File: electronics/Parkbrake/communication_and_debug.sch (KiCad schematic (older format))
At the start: 18 parts

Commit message: ordernr, type and footprints for all components
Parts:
- C? (x3): footprint (none) -> Capacitors_SMD:C_0805; farnell (none) -> 2496940; part (none) -> 0805B104J500CT
- C?: footprint (none) -> Capacitors_SMD:C_0805; farnell (none) -> 2494247; part (none) -> GRM2165C1H102JA01D
- R?: farnell (none) -> 9332480; part (none) -> MC01W08051120R
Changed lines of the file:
@@
 F 0 "C?" H 2475 3550 50  0000 L CNN
 F 1 "100n" H 2475 3350 50  0000 L CNN
-F 2 "" H 2488 3300 50  0000 C CNN
+F 2 "Capacitors_SMD:C_0805" H 2488 3300 50  0001 C CNN
 F 3 "" H 2450 3450 50  0000 C CNN
+F 4 "2496940" H 2450 3450 60  0001 C CNN "farnell"
+F 5 "0805B104J500CT" H 2450 3450 60  0001 C CNN "part"
 	1    2450 3450
 	1    0    0    -1
@@
 F 0 "C?" H 2725 3550 50  0000 L CNN
 F 1 "1n" H 2725 3350 50  0000 L CNN
-F 2 "" H 2738 3300 50  0000 C CNN
+F 2 "Capacitors_SMD:C_0805" H 2738 3300 50  0001 C CNN
 F 3 "" H 2700 3450 50  0000 C CNN
+F 4 "2494247" H 2700 3450 60  0001 C CNN "farnell"
+F 5 "GRM2165C1H102JA01D" H 2700 3450 60  0001 C CNN "part"
 	1    2700 3450
 	1    0    0    -1
@@
 F 0 "C?" H 3450 4525 50  0000 L CNN
 F 1 "100n" H 3450 4325 50  0000 L CNN
-F 2 "" H 3463 4275 50  0000 C CNN
+F 2 "Capacitors_SMD:C_0805" H 3463 4275 50  0001 C CNN
 F 3 "" H 3425 4425 50  0000 C CNN
+F 4 "2496940" H 3425 4425 60  0001 C CNN "farnell"
+F 5 "0805B104J500CT" H 3425 4425 60  0001 C CNN "part"
 	1    3425 4425
 	1    0    0    -1
@@
 F 2 "" V 3505 4050 50  0000 C CNN
 F 3 "" H 3575 4050 50  0000 C CNN
+F 4 "MC01W08051120R" V 3575 4050 60  0001 C CNN "part"
+F 5 "9332480" V 3575 4050 60  0001 C CNN "farnell"
 	1    3575 4050
 	1    0    0    -1
@@
 F 0 "C?" H 7900 5200 50  0000 L CNN
 F 1 "100n" H 7900 5000 50  0000 L CNN
-F 2 "" H 7913 4950 50  0000 C CNN
+F 2 "Capacitors_SMD:C_0805" H 7913 4950 50  0001 C CNN
 F 3 "" H 7875 5100 50  0000 C CNN
+F 4 "2496940" H 7875 5100 60  0001 C CNN "farnell"
+F 5 "0805B104J500CT" H 7875 5100 60  0001 C CNN "part"
 	1    7875 5100
 	1    0    0    -1

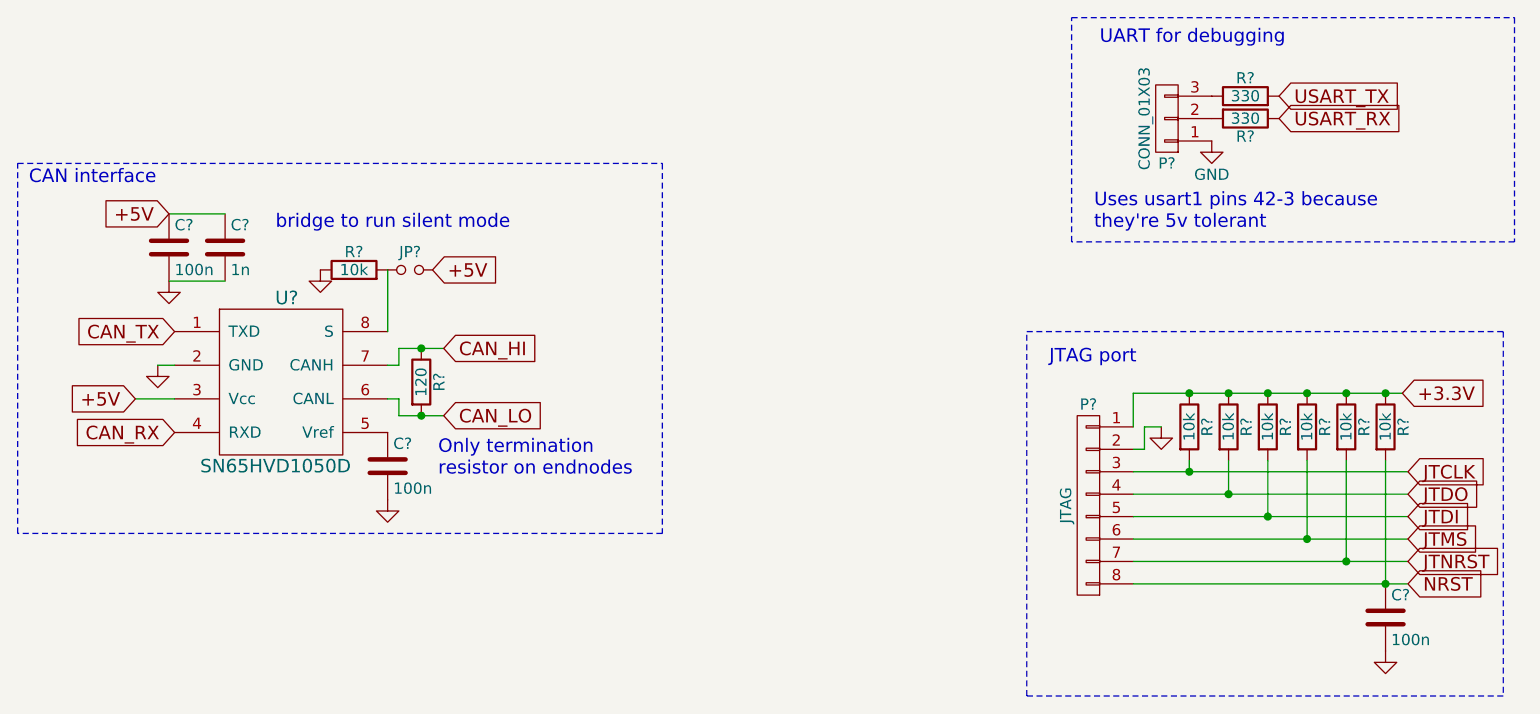
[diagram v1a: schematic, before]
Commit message: Make it pass DRC rule check
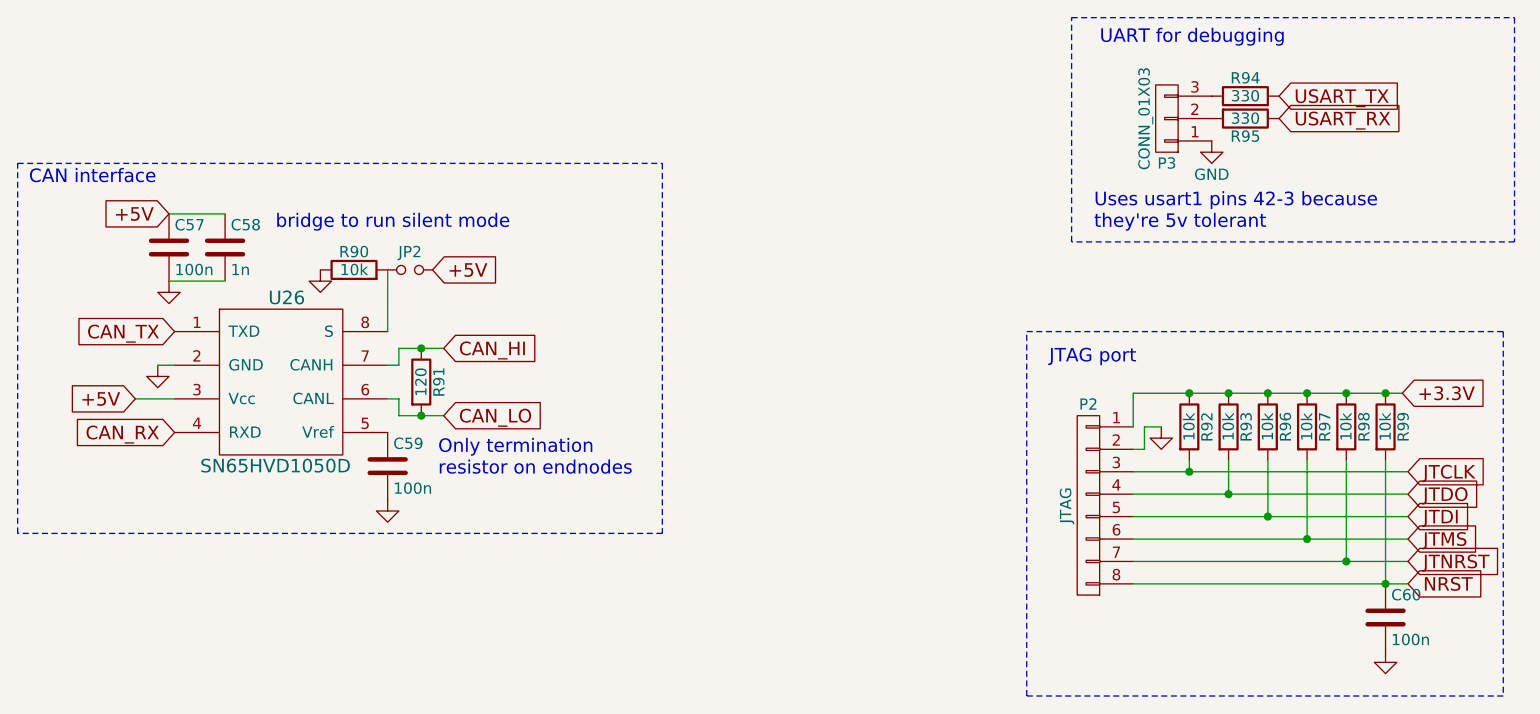
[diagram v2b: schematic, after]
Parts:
- gave numbers to parts that had none: 18
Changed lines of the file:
@@
 $EndDescr
 $Comp
-L SN65HVD1050D U?
+L SN65HVD1050D U26
 U 1 1 5791E80E
 P 2925 4025
-F 0 "U?" H 2975 4375 60  0000 C CNN
+F 0 "U26" H 2975 4375 60  0000 C CNN
 F 1 "SN65HVD1050D" H 2925 3625 60  0000 C CNN
 F 2 "Housings_SOIC:SOIC-8_3.9x4.9mm_Pitch1.27mm" H 3025 3875 60  0001 C CNN
@@
 $EndComp
 $Comp
-L R R?
+L R R90
 U 1 1 5791E8BD
 P 3275 3550
-F 0 "R?" V 3355 3550 50  0000 C CNN
+F 0 "R90" V 3355 3550 50  0000 C CNN
 F 1 "10k" V 3275 3550 50  0000 C CNN
 F 2 "Resistors_SMD:R_0805" V 3205 3550 50  0001 C CNN
@@
 $EndComp
 $Comp
-L Jumper_NO_Small JP?
+L Jumper_NO_Small JP2
 U 1 1 5791E904
 P 3525 3550
-F 0 "JP?" H 3525 3630 50  0000 C CNN
+F 0 "JP2" H 3525 3630 50  0000 C CNN
 F 1 "Jumper_NO_Small" H 3535 3490 50  0001 C CNN
 F 2 "" H 3525 3550 50  0000 C CNN
@@
 $EndComp
 $Comp
-L GND #PWR?
+L GND #PWR082
 U 1 1 5791E9C0
 P 3125 3550
-F 0 "#PWR?" H 3125 3300 50  0001 C CNN
+F 0 "#PWR082" H 3125 3300 50  0001 C CNN
 F 1 "GND" H 3125 3400 50  0001 C CNN
 F 2 "" H 3125 3550 50  0000 C CNN
@@
 $EndComp
 $Comp
-L C C?
+L C C57
 U 1 1 5791E9E8
 P 2450 3450
-F 0 "C?" H 2475 3550 50  0000 L CNN
+F 0 "C57" H 2475 3550 50  0000 L CNN
 F 1 "100n" H 2475 3350 50  0000 L CNN
 F 2 "Capacitors_SMD:C_0805" H 2488 3300 50  0001 C CNN
@@
 $EndComp
 $Comp
-L C C?
+L C C58
 U 1 1 5791EA0D
 P 2700 3450
-F 0 "C?" H 2725 3550 50  0000 L CNN
+F 0 "C58" H 2725 3550 50  0000 L CNN
 F 1 "1n" H 2725 3350 50  0000 L CNN
 F 2 "Capacitors_SMD:C_0805" H 2738 3300 50  0001 C CNN
@@
 	2700 3600 2450 3600
 $Comp
-L GND #PWR?
+L GND #PWR083
 U 1 1 5791EA76
 P 2450 3600
-F 0 "#PWR?" H 2450 3350 50  0001 C CNN
+F 0 "#PWR083" H 2450 3350 50  0001 C CNN
 F 1 "GND" H 2450 3450 50  0001 C CNN
 F 2 "" H 2450 3600 50  0000 C CNN
@@
 +5V
 $Comp
-L GND #PWR?
+L GND #PWR084
 U 1 1 5791EABC
 P 2400 3975
-F 0 "#PWR?" H 2400 3725 50  0001 C CNN
+F 0 "#PWR084" H 2400 3725 50  0001 C CNN
 F 1 "GND" H 2400 3825 50  0001 C CNN
 F 2 "" H 2400 3975 50  0000 C CNN
@@
 	2475 4125 2300 4125
 $Comp
-L C C?
+L C C59
 U 1 1 5791EB00
 P 3425 4425
-F 0 "C?" H 3450 4525 50  0000 L CNN
+F 0 "C59" H 3450 4525 50  0000 L CNN
 F 1 "100n" H 3450 4325 50  0000 L CNN
 F 2 "Capacitors_SMD:C_0805" H 3463 4275 50  0001 C CNN
@@
 $EndComp
 $Comp
-L GND #PWR?
+L GND #PWR085
 U 1 1 5791EB6A
 P 3425 4575
-F 0 "#PWR?" H 3425 4325 50  0001 C CNN
+F 0 "#PWR085" H 3425 4325 50  0001 C CNN
 F 1 "GND" H 3425 4425 50  0001 C CNN
 F 2 "" H 3425 4575 50  0000 C CNN
@@
 bridge to run silent mode
 $Comp
-L R R?
+L R R91
 U 1 1 5791F232
 P 3575 4050
-F 0 "R?" V 3655 4050 50  0000 C CNN
+F 0 "R91" V 3655 4050 50  0000 C CNN
 F 1 "120" V 3575 4050 50  0000 C CNN
 F 2 "" V 3505 4050 50  0000 C CNN
@@
 Connection ~ 3575 3900
 $Comp
-L CONN_01X03 P?
+L CONN_01X03 P3
 U 1 1 57920C75
 P 6900 2875
-F 0 "P?" H 6900 3075 50  0000 C CNN
+F 0 "P3" H 6900 3075 50  0000 C CNN
 F 1 "CONN_01X03" V 7000 2875 50  0000 C CNN
 F 2 "" H 6900 2875 50  0000 C CNN
@@
 $EndComp
 $Comp
-L R R?
+L R R94
 U 1 1 57920D82
 P 7250 2775
-F 0 "R?" V 7330 2775 50  0000 C CNN
+F 0 "R94" V 7330 2775 50  0000 C CNN
 F 1 "330" V 7250 2775 50  0000 C CNN
 F 2 "" V 7180 2775 50  0000 C CNN
@@
 $EndComp
 $Comp
-L R R?
+L R R95
 U 1 1 57920DB5
 P 7250 2875
-F 0 "R?" V 7330 2875 50  0000 C CNN
+F 0 "R95" V 7330 2875 50  0000 C CNN
 F 1 "330" V 7250 2875 50  0000 C CNN
 F 2 "" V 7180 2875 50  0000 C CNN
@@
 $EndComp
 $Comp
-L GND #PWR?
+L GND #PWR086
 U 1 1 57920F20
 P 7100 2975
-F 0 "#PWR?" H 7100 2725 50  0001 C CNN
+F 0 "#PWR086" H 7100 2725 50  0001 C CNN
 F 1 "GND" H 7100 2825 50  0000 C CNN
 F 2 "" H 7100 2975 50  0000 C CNN
@@
 	6475 3425 6475 2425
 $Comp
-L GND #PWR?
+L GND #PWR087
 U 1 1 579225C8
 P 6875 4250
-F 0 "#PWR?" H 6875 4000 50  0001 C CNN
+F 0 "#PWR087" H 6875 4000 50  0001 C CNN
 F 1 "GND" H 6875 4100 50  0001 C CNN
 F 2 "" H 6875 4250 50  0000 C CNN
@@
 +3.3V
 $Comp
-L CONN_01X08 P?
+L CONN_01X08 P2
 U 1 1 57922780
 P 6550 4600
-F 0 "P?" H 6550 5050 50  0000 C CNN
+F 0 "P2" H 6550 5050 50  0000 C CNN
 F 1 "JTAG" V 6650 4600 50  0000 C CNN
 F 2 "" H 6550 4600 50  0000 C CNN
@@
 JTAG port
 $Comp
-L R R?
+L R R92
 U 1 1 5792478C
 P 7000 4250
-F 0 "R?" V 7080 4250 50  0000 C CNN
+F 0 "R92" V 7080 4250 50  0000 C CNN
 F 1 "10k" V 7000 4250 50  0000 C CNN
 F 2 "Resistors_SMD:R_0805" V 6930 4250 50  0001 C CNN
@@
 	6800 4250 6875 4250
 $Comp
-L R R?
+L R R93
 U 1 1 57924D13
 P 7175 4250
-F 0 "R?" V 7255 4250 50  0000 C CNN
+F 0 "R93" V 7255 4250 50  0000 C CNN
 F 1 "10k" V 7175 4250 50  0000 C CNN
 F 2 "Resistors_SMD:R_0805" V 7105 4250 50  0001 C CNN
@@
 $EndComp
 $Comp
-L R R?
+L R R96
 U 1 1 57924D64
 P 7350 4250
-F 0 "R?" V 7430 4250 50  0000 C CNN
+F 0 "R96" V 7430 4250 50  0000 C CNN
 F 1 "10k" V 7350 4250 50  0000 C CNN
 F 2 "Resistors_SMD:R_0805" V 7280 4250 50  0001 C CNN
@@
 $EndComp
 $Comp
-L R R?
+L R R97
 U 1 1 57924DA8
 P 7525 4250
-F 0 "R?" V 7605 4250 50  0000 C CNN
+F 0 "R97" V 7605 4250 50  0000 C CNN
 F 1 "10k" V 7525 4250 50  0000 C CNN
 F 2 "Resistors_SMD:R_0805" V 7455 4250 50  0001 C CNN
@@
 $EndComp
 $Comp
-L R R?
+L R R98
 U 1 1 57924E03
 P 7700 4250
-F 0 "R?" V 7780 4250 50  0000 C CNN
+F 0 "R98" V 7780 4250 50  0000 C CNN
 F 1 "10k" V 7700 4250 50  0000 C CNN
 F 2 "Resistors_SMD:R_0805" V 7630 4250 50  0001 C CNN
@@
 Connection ~ 7700 4850
 $Comp
-L R R?
+L R R99
 U 1 1 5792546C
 P 7875 4250
-F 0 "R?" V 7955 4250 50  0000 C CNN
+F 0 "R99" V 7955 4250 50  0000 C CNN
 F 1 "10k" V 7875 4250 50  0000 C CNN
 F 2 "Resistors_SMD:R_0805" V 7805 4250 50  0001 C CNN
@@
 Connection ~ 7875 4100
 $Comp
-L C C?
+L C C60
 U 1 1 579264A6
 P 7875 5100
-F 0 "C?" H 7900 5200 50  0000 L CNN
+F 0 "C60" H 7900 5200 50  0000 L CNN
 F 1 "100n" H 7900 5000 50  0000 L CNN
 F 2 "Capacitors_SMD:C_0805" H 7913 4950 50  0001 C CNN
@@
 $EndComp
 $Comp
-L GND #PWR?
+L GND #PWR088
 U 1 1 579264FD
 P 7875 5250
-F 0 "#PWR?" H 7875 5000 50  0001 C CNN
+F 0 "#PWR088" H 7875 5000 50  0001 C CNN
 F 1 "GND" H 7875 5100 50  0001 C CNN
 F 2 "" H 7875 5250 50  0000 C CNN

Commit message: More fixes and chenged components eat less boardspace
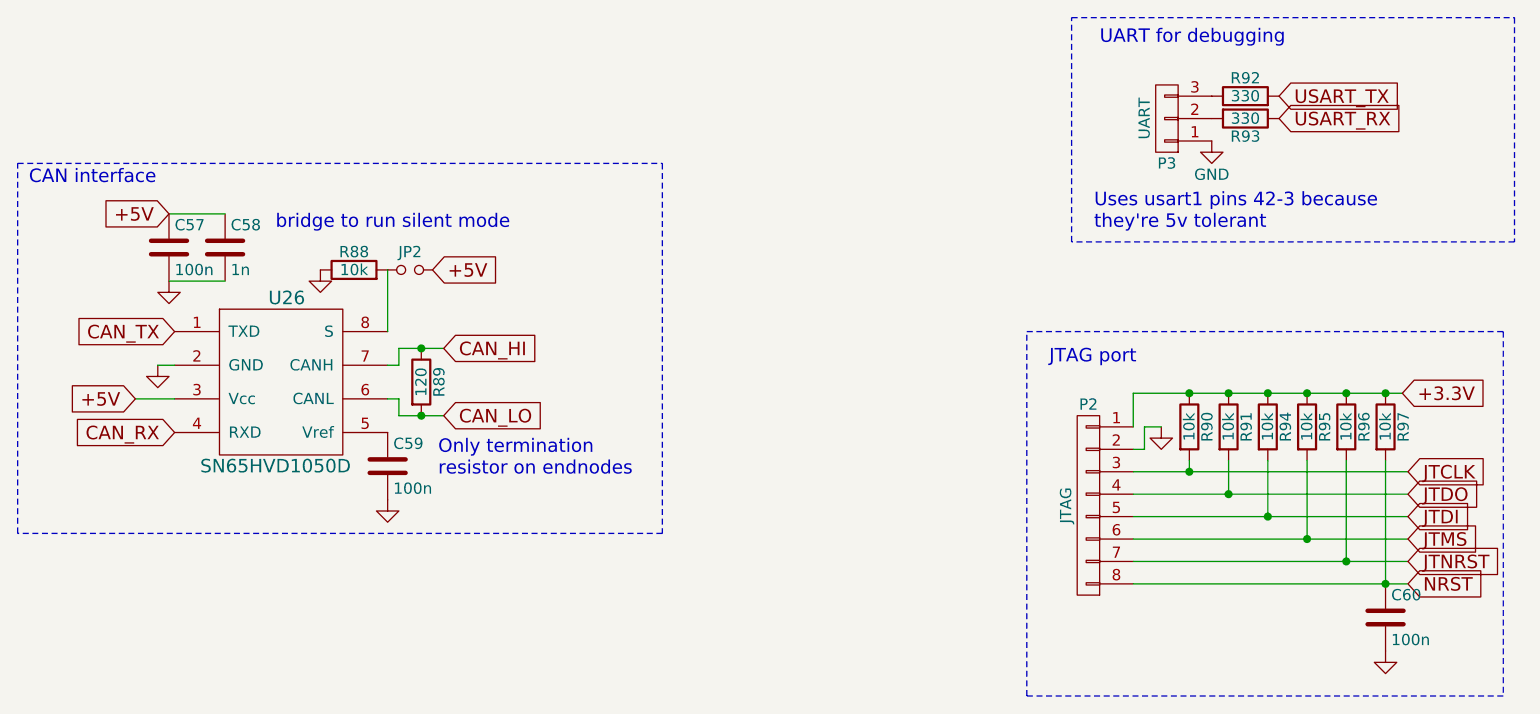
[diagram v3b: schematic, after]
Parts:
- JP2: footprint (none) -> Resistors_SMD:R_0805_HandSoldering; farnell (none) -> 9240276; part (none) -> RC1206JR-070RL
- P2: footprint (none) -> Socket_Strips:Socket_Strip_Straight_1x08; farnell (none) -> 2356160; part (none) -> 61300811121
- P3: value CONN_01X03 -> UART; footprint (none) -> Socket_Strips:Socket_Strip_Straight_1x03; farnell (none) -> 3418297; part (none) -> 826629-3
- R89: renamed from R91; footprint (none) -> Resistors_SMD:R_0805
- R92: renamed from R94; footprint (none) -> Resistors_SMD:R_0805
- R93: renamed from R95; footprint (none) -> Resistors_SMD:R_0805
- renumbered R90 to R88, R92 to R90, R93 to R91, R96 to R94, R97 to R95, R98 to R96, R99 to R97
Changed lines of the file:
@@
 $EndComp
 $Comp
-L R R90
+L R R88
 U 1 1 5791E8BD
 P 3275 3550
-F 0 "R90" V 3355 3550 50  0000 C CNN
+F 0 "R88" V 3355 3550 50  0000 C CNN
 F 1 "10k" V 3275 3550 50  0000 C CNN
 F 2 "Resistors_SMD:R_0805" V 3205 3550 50  0001 C CNN
@@
 F 0 "JP2" H 3525 3630 50  0000 C CNN
 F 1 "Jumper_NO_Small" H 3535 3490 50  0001 C CNN
-F 2 "" H 3525 3550 50  0000 C CNN
+F 2 "Resistors_SMD:R_0805_HandSoldering" H 3525 3550 50  0001 C CNN
 F 3 "" H 3525 3550 50  0000 C CNN
+F 4 "RC1206JR-070RL" H 3525 3550 60  0001 C CNN "part"
+F 5 "9240276" H 3525 3550 60  0001 C CNN "farnell"
 	1    3525 3550
 	1    0    0    -1
 $EndComp
 $Comp
-L GND #PWR082
+L GND #PWR77
 U 1 1 5791E9C0
 P 3125 3550
-F 0 "#PWR082" H 3125 3300 50  0001 C CNN
+F 0 "#PWR77" H 3125 3300 50  0001 C CNN
 F 1 "GND" H 3125 3400 50  0001 C CNN
 F 2 "" H 3125 3550 50  0000 C CNN
@@
 	2700 3600 2450 3600
 $Comp
-L GND #PWR083
+L GND #PWR76
 U 1 1 5791EA76
 P 2450 3600
-F 0 "#PWR083" H 2450 3350 50  0001 C CNN
+F 0 "#PWR76" H 2450 3350 50  0001 C CNN
 F 1 "GND" H 2450 3450 50  0001 C CNN
 F 2 "" H 2450 3600 50  0000 C CNN
@@
 +5V
 $Comp
-L GND #PWR084
+L GND #PWR75
 U 1 1 5791EABC
 P 2400 3975
-F 0 "#PWR084" H 2400 3725 50  0001 C CNN
+F 0 "#PWR75" H 2400 3725 50  0001 C CNN
 F 1 "GND" H 2400 3825 50  0001 C CNN
 F 2 "" H 2400 3975 50  0000 C CNN
@@
 $EndComp
 $Comp
-L GND #PWR085
+L GND #PWR78
 U 1 1 5791EB6A
 P 3425 4575
-F 0 "#PWR085" H 3425 4325 50  0001 C CNN
+F 0 "#PWR78" H 3425 4325 50  0001 C CNN
 F 1 "GND" H 3425 4425 50  0001 C CNN
 F 2 "" H 3425 4575 50  0000 C CNN
@@
 bridge to run silent mode
 $Comp
-L R R91
+L R R89
 U 1 1 5791F232
 P 3575 4050
-F 0 "R91" V 3655 4050 50  0000 C CNN
+F 0 "R89" V 3655 4050 50  0000 C CNN
 F 1 "120" V 3575 4050 50  0000 C CNN
-F 2 "" V 3505 4050 50  0000 C CNN
+F 2 "Resistors_SMD:R_0805" V 3505 4050 50  0001 C CNN
 F 3 "" H 3575 4050 50  0000 C CNN
 F 4 "MC01W08051120R" V 3575 4050 60  0001 C CNN "part"
@@
 P 6900 2875
 F 0 "P3" H 6900 3075 50  0000 C CNN
-F 1 "CONN_01X03" V 7000 2875 50  0000 C CNN
-F 2 "" H 6900 2875 50  0000 C CNN
+F 1 "UART" V 7000 2875 50  0000 C CNN
+F 2 "Socket_Strips:Socket_Strip_Straight_1x03" H 6900 2875 50  0001 C CNN
 F 3 "" H 6900 2875 50  0000 C CNN
+F 4 "826629-3" H 6900 2875 60  0001 C CNN "part"
+F 5 "3418297" H 6900 2875 60  0001 C CNN "farnell"
 	1    6900 2875
 	-1   0    0    1
 $EndComp
 $Comp
-L R R94
+L R R92
 U 1 1 57920D82
 P 7250 2775
-F 0 "R94" V 7330 2775 50  0000 C CNN
+F 0 "R92" V 7330 2775 50  0000 C CNN
 F 1 "330" V 7250 2775 50  0000 C CNN
-F 2 "" V 7180 2775 50  0000 C CNN
+F 2 "Resistors_SMD:R_0805" V 7180 2775 50  0001 C CNN
 F 3 "" H 7250 2775 50  0000 C CNN
 F 4 "MC01W08051330R" V 7250 2775 60  0001 C CNN "part"
@@
 $EndComp
 $Comp
-L R R95
+L R R93
 U 1 1 57920DB5
 P 7250 2875
-F 0 "R95" V 7330 2875 50  0000 C CNN
+F 0 "R93" V 7330 2875 50  0000 C CNN
 F 1 "330" V 7250 2875 50  0000 C CNN
-F 2 "" V 7180 2875 50  0000 C CNN
+F 2 "Resistors_SMD:R_0805" V 7180 2875 50  0001 C CNN
 F 3 "" H 7250 2875 50  0000 C CNN
 F 4 "MC01W08051330R" V 7250 2875 60  0001 C CNN "part"
@@
 $EndComp
 $Comp
-L GND #PWR086
+L GND #PWR80
 U 1 1 57920F20
 P 7100 2975
-F 0 "#PWR086" H 7100 2725 50  0001 C CNN
+F 0 "#PWR80" H 7100 2725 50  0001 C CNN
 F 1 "GND" H 7100 2825 50  0000 C CNN
 F 2 "" H 7100 2975 50  0000 C CNN
@@
 	6475 3425 6475 2425
 $Comp
-L GND #PWR087
+L GND #PWR79
 U 1 1 579225C8
 P 6875 4250
-F 0 "#PWR087" H 6875 4000 50  0001 C CNN
+F 0 "#PWR79" H 6875 4000 50  0001 C CNN
 F 1 "GND" H 6875 4100 50  0001 C CNN
 F 2 "" H 6875 4250 50  0000 C CNN
@@
 F 0 "P2" H 6550 5050 50  0000 C CNN
 F 1 "JTAG" V 6650 4600 50  0000 C CNN
-F 2 "" H 6550 4600 50  0000 C CNN
+F 2 "Socket_Strips:Socket_Strip_Straight_1x08" H 6550 4600 50  0001 C CNN
 F 3 "" H 6550 4600 50  0000 C CNN
+F 4 "61300811121" H 6550 4600 60  0001 C CNN "part"
+F 5 "2356160" H 6550 4600 60  0001 C CNN "farnell"
 	1    6550 4600
 	-1   0    0    -1
@@
 JTAG port
 $Comp
-L R R92
+L R R90
 U 1 1 5792478C
 P 7000 4250
-F 0 "R92" V 7080 4250 50  0000 C CNN
+F 0 "R90" V 7080 4250 50  0000 C CNN
 F 1 "10k" V 7000 4250 50  0000 C CNN
 F 2 "Resistors_SMD:R_0805" V 6930 4250 50  0001 C CNN
@@
 	6800 4250 6875 4250
 $Comp
-L R R93
+L R R91
 U 1 1 57924D13
 P 7175 4250
-F 0 "R93" V 7255 4250 50  0000 C CNN
+F 0 "R91" V 7255 4250 50  0000 C CNN
 F 1 "10k" V 7175 4250 50  0000 C CNN
 F 2 "Resistors_SMD:R_0805" V 7105 4250 50  0001 C CNN
@@
 $EndComp
 $Comp
-L R R96
+L R R94
 U 1 1 57924D64
 P 7350 4250
-F 0 "R96" V 7430 4250 50  0000 C CNN
+F 0 "R94" V 7430 4250 50  0000 C CNN
 F 1 "10k" V 7350 4250 50  0000 C CNN
 F 2 "Resistors_SMD:R_0805" V 7280 4250 50  0001 C CNN
@@
 $EndComp
 $Comp
-L R R97
+L R R95
 U 1 1 57924DA8
 P 7525 4250
-F 0 "R97" V 7605 4250 50  0000 C CNN
+F 0 "R95" V 7605 4250 50  0000 C CNN
 F 1 "10k" V 7525 4250 50  0000 C CNN
 F 2 "Resistors_SMD:R_0805" V 7455 4250 50  0001 C CNN
@@
 $EndComp
 $Comp
-L R R98
+L R R96
 U 1 1 57924E03
 P 7700 4250
-F 0 "R98" V 7780 4250 50  0000 C CNN
+F 0 "R96" V 7780 4250 50  0000 C CNN
 F 1 "10k" V 7700 4250 50  0000 C CNN
 F 2 "Resistors_SMD:R_0805" V 7630 4250 50  0001 C CNN
@@
 Connection ~ 7700 4850
 $Comp
-L R R99
+L R R97
 U 1 1 5792546C
 P 7875 4250
-F 0 "R99" V 7955 4250 50  0000 C CNN
+F 0 "R97" V 7955 4250 50  0000 C CNN
 F 1 "10k" V 7875 4250 50  0000 C CNN
 F 2 "Resistors_SMD:R_0805" V 7805 4250 50  0001 C CNN
@@
 $EndComp
 $Comp
-L GND #PWR088
+L GND #PWR81
 U 1 1 579264FD
 P 7875 5250
-F 0 "#PWR088" H 7875 5000 50  0001 C CNN
+F 0 "#PWR81" H 7875 5000 50  0001 C CNN
 F 1 "GND" H 7875 5100 50  0001 C CNN
 F 2 "" H 7875 5250 50  0000 C CNN
